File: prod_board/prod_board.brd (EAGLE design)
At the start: 160 x 100 mm, 31 parts

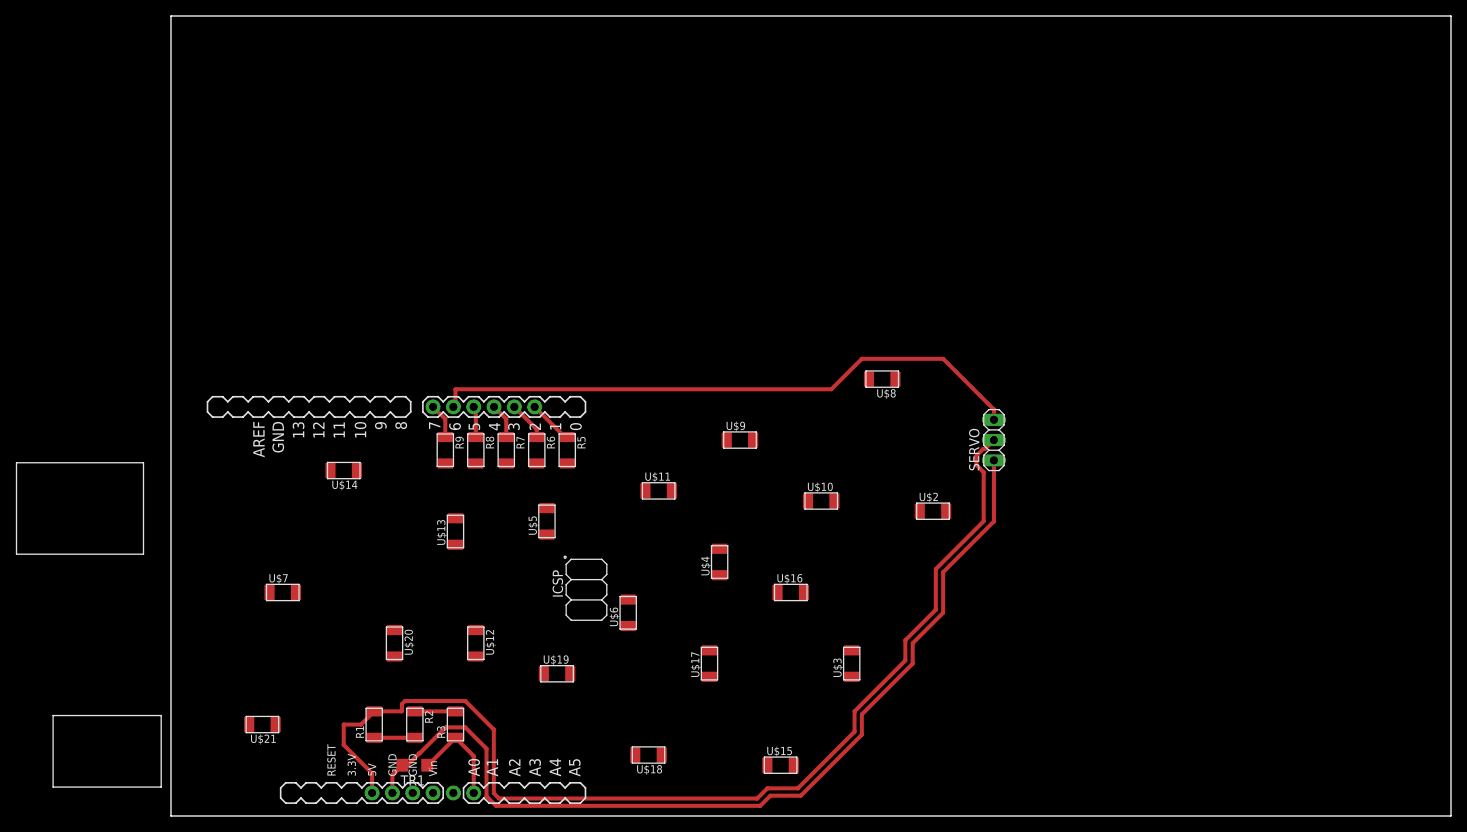
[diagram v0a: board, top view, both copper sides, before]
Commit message: main board into production v1
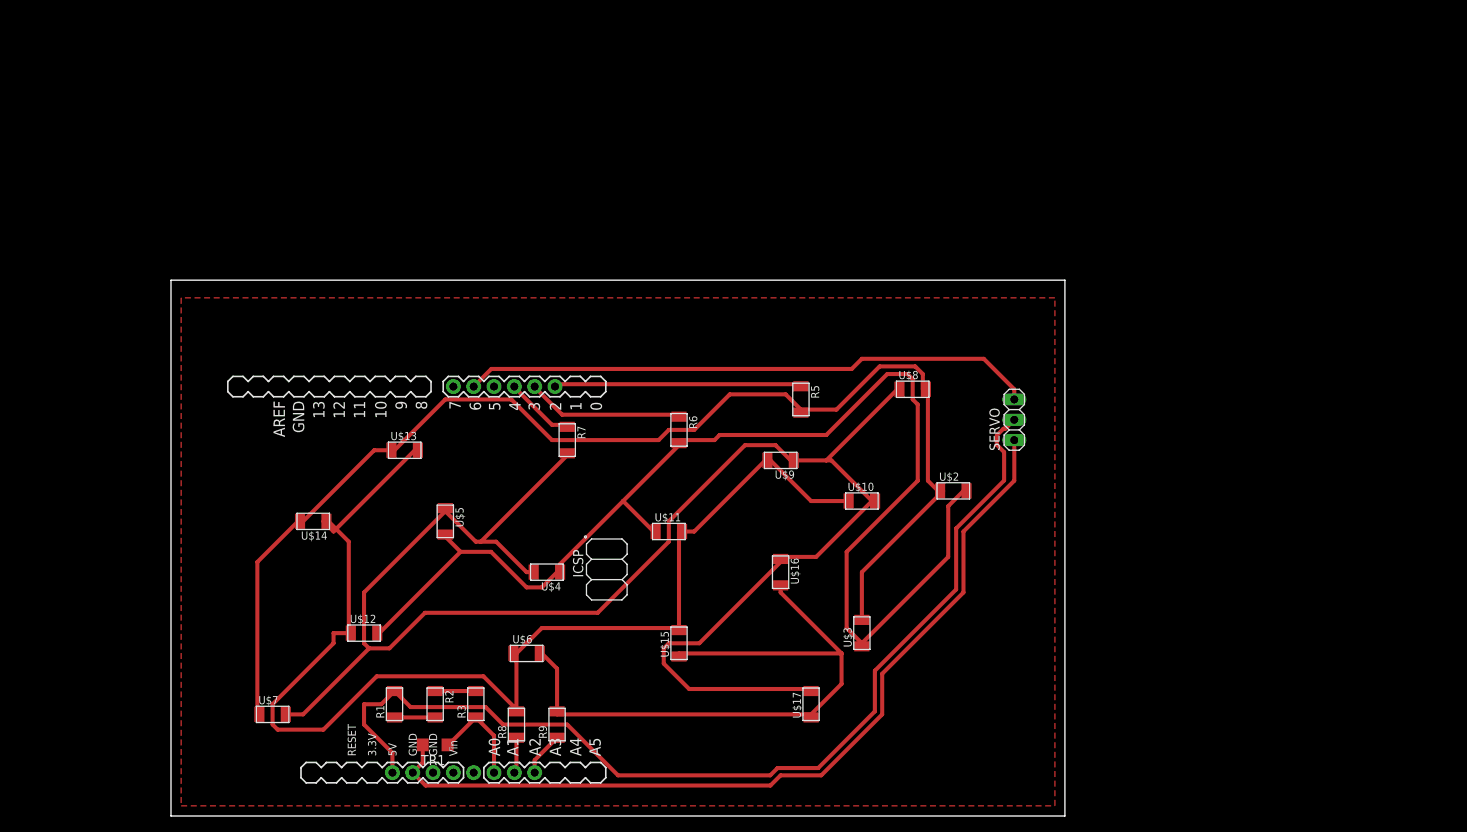
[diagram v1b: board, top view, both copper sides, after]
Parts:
- removed U$18, U$19, U$20, U$21: LEDFAB1206, fab:LED1206FAB
- moved R9 37.0 mm to (48.3, 11.4), turned to 90 degrees
- moved R8 34.7 mm to (43.2, 11.4), turned to 90 degrees
- moved R5 29.9 mm to (78.7, 52.1)
- moved U$4 21.6 mm to (47.0, 30.5), turned to 180 degrees
- moved U$15 19.8 mm to (63.5, 21.6), turned to 90 degrees
- moved R6 18.0 mm to (63.5, 48.3)
- moved U$7 15.3 mm to (12.7, 12.7)
- moved U$12 14.0 mm to (24.1, 22.9), turned to 0 degrees
- moved U$17 13.7 mm to (80.0, 14.0)
- moved U$6 13.7 mm to (44.5, 20.3), turned to 0 degrees
- moved U$5 12.7 mm to (34.3, 36.8), turned to 270 degrees
- moved U$13 12.0 mm to (29.2, 45.7), turned to 0 degrees
- moved R7 7.73 mm to (49.5, 47.0)
- moved U$14 7.41 mm to (17.8, 36.8)
- moved U$9 5.68 mm to (76.2, 44.5), turned to 180 degrees
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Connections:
- removed net N$9: R9.2, U$15.1, U$16.2, U$17.1, U$18.2, U$19.1, U$20.2, U$21.1, U$6.2
- new net N$15: R9.2, U$15.1, U$16.2, U$17.1, U$6.2
- net N$12: now also U$22.A1; no longer U$22.5
- net N$13: now also U$22.A2; no longer U$22.7
- net N$5: no longer U$20.1, U$21.2
- net N$6: no longer U$18.1, U$19.2
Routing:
- net N$7: track 0.00 -> 212.5 mm
- net N$6: track 0.00 -> 156.7 mm
- net N$5: track 0.00 -> 155.9 mm
- net N$8: track 0.00 -> 152.7 mm
- net N$15: track 0.00 -> 82.4 mm
- net N$3: track 5.63 -> 31.1 mm
- net N$10: track 4.93 -> 19.8 mm
- net GND: track 115.7 -> 108.1 mm
- net +5V: track 133.3 -> 126.8 mm
- net N$11: track 4.40 -> 8.87 mm
- net N$14: track 75.1 -> 71.9 mm
- net N$13: track 4.40 -> 5.52 mm
- net N$12: track 3.88 -> 4.47 mm
- added copper zone on layer 1, net N$9
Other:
- board size 160 x 100 mm -> 111.7 x 67 mm
